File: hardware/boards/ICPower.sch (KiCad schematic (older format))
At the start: 39 parts, among them U1 ECP5UM5G-381caBGA, U3 CYUSB3014, U4 IS43TR16256B-125KBL, U5 128MiB, U6 128MiB

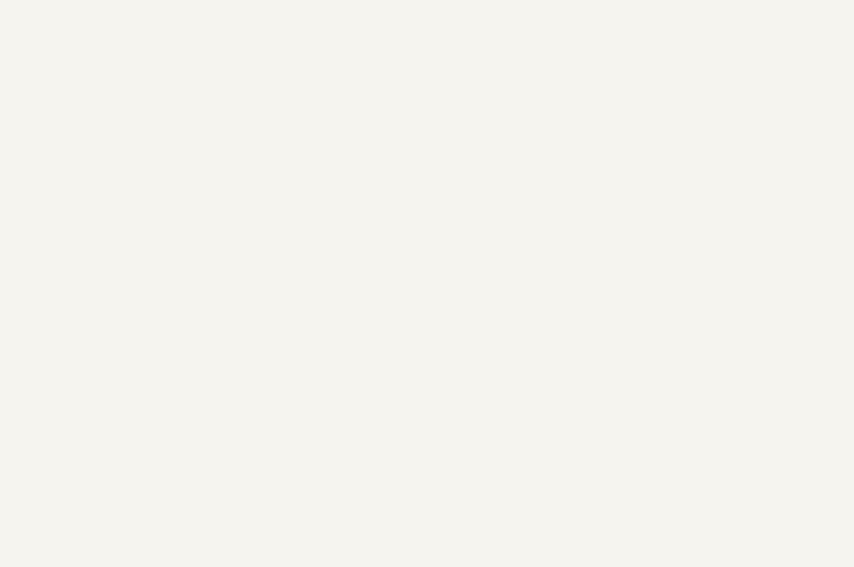
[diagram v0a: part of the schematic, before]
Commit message: Added a clock fanout buffer for the PCIe REFCLOCK to connect to the FPGAs SERDES banks
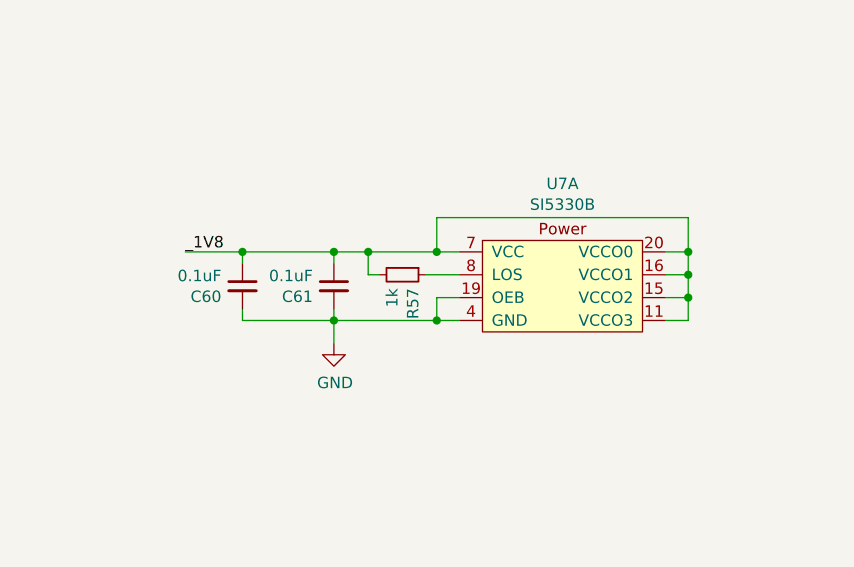
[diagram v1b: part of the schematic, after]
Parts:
- added C60, C61: 0.1uF, Capacitor_SMD:C_0603_1608Metric, symbol Device:C_Small
- added R57: 1k, Resistor_SMD:R_0603_1608Metric, symbol Device:R_Small
- added U7: SI5330B, Package_DFN_QFN:VQFN-24-1EP_4x4mm_P0.5mm_EP2.45x2.45mm, symbol lethalbit:SI5330B
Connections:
- net 1V8: now also C60.1, C61.1, R57.2, U7.11 (VCCO3), U7.15 (VCCO2), U7.16 (VCCO1), U7.20 (VCCO0), U7.24 (VCC), U7.7 (VCC)
- net GND: now also C60.2, C61.2, U7.12 (GND), U7.19 (OEB), U7.23 (GND), U7.25 (GND), U7.4 (GND), U7.5 (GND), U7.6 (GND)
- new net: R57.1, U7.8 (LOS)
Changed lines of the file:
@@
 Wire Wire Line
 	6400 4700 6650 4700
+$Comp
+L lethalbit:SI5330B U7
+U 1 1 5F1C6134
+P 5250 8250
+F 0 "U7" H 5250 8648 50  0000 C CNN
+F 1 "SI5330B" H 5250 8557 50  0000 C CNN
+F 2 "Package_DFN_QFN:VQFN-24-1EP_4x4mm_P0.5mm_EP2.45x2.45mm" H 5250 8550 50  0001 C CNN
+F 3 "https://www.silabs.com/documents/public/data-sheets/Si5330.pdf" H 5250 8550 50  0001 C CNN
+F 4 "Silicon Labs" H 5250 8250 50  0001 C CNN "MFR"
+F 5 "SI5330B-B00205-GM" H 5250 8250 50  0001 C CNN "MPN"
+	1    5250 8250
+	1    0    0    -1
+$EndComp
+$Comp
+L power:GND #PWR0141
+U 1 1 5F1E08C0
+P 4250 8550
+F 0 "#PWR0141" H 4250 8300 50  0001 C CNN
+F 1 "GND" H 4255 8377 50  0000 C CNN
+F 2 "" H 4250 8550 50  0001 C CNN
+F 3 "" H 4250 8550 50  0001 C CNN
+	1    4250 8550
+	1    0    0    -1
+$EndComp
+Wire Wire Line
+	4800 8450 4700 8450
+Wire Wire Line
+	4250 8450 4250 8550
+$Comp
+L Device:C_Small C?
+U 1 1 5F1EFE73
+P 4250 8300
+AR Path="/5EDF9F51/5F1EFE73" Ref="C?"  Part="1"
+AR Path="/5EF66188/5F1EFE73" Ref="C61"  Part="1"
+F 0 "C61" H 4158 8254 50  0000 R CNN
+F 1 "0.1uF" H 4158 8345 50  0000 R CNN
+F 2 "Capacitor_SMD:C_0603_1608Metric" H 4250 8300 50  0001 C CNN
+F 3 "~" H 4250 8300 50  0001 C CNN
+F 4 "KEMET" V 4250 8300 50  0001 C CNN "MFR"
+F 5 "C0603C104M5RACTU" V 4250 8300 50  0001 C CNN "MPN"
+	1    4250 8300
+	1    0    0    -1
+$EndComp
+Wire Wire Line
+	4250 8400 4250 8450
+Wire Wire Line
+	4250 8200 4250 8150
+Wire Wire Line
+	4250 8150 4400 8150
+Wire Wire Line
+	4250 8150 3850 8150
+Connection ~ 4250 8150
+Text Label 3600 8150 0    50   ~ 0
+_1V8
+Wire Wire Line
+	4700 8150 4700 8000
+Wire Wire Line
+	4700 8000 5800 8000
+Wire Wire Line
+	5800 8000 5800 8150
+Wire Wire Line
+	5800 8450 5700 8450
+Connection ~ 4700 8150
+Wire Wire Line
+	4700 8150 4800 8150
+Wire Wire Line
+	5800 8350 5700 8350
+Connection ~ 5800 8350
+Wire Wire Line
+	5800 8350 5800 8450
+Wire Wire Line
+	5800 8250 5700 8250
+Connection ~ 5800 8250
+Wire Wire Line
+	5800 8250 5800 8350
+Wire Wire Line
+	5800 8150 5700 8150
+Connection ~ 5800 8150
+Wire Wire Line
+	5800 8150 5800 8250
+$Comp
+L Device:R_Small R?
+U 1 1 5F29D318
+P 4550 8250
+AR Path="/5EF66251/5F29D318" Ref="R?"  Part="1"
+AR Path="/5EF66188/5F29D318" Ref="R57"  Part="1"
+F 0 "R57" H 4609 8296 50  0000 L CNN
+F 1 "1k" H 4609 8205 50  0000 L CNN
+F 2 "Resistor_SMD:R_0603_1608Metric" H 4550 8250 50  0001 C CNN
+F 3 "~" H 4550 8250 50  0001 C CNN
+F 4 "Vishay Dale" H 4550 8250 50  0001 C CNN "MFR"
+F 5 "CRCW06031K00FKEAHP" H 4550 8250 50  0001 C CNN "MPN"
+	1    4550 8250
+	0    1    1    0
+$EndComp
+Connection ~ 4250 8450
+Wire Wire Line
+	4400 8150 4400 8250
+Wire Wire Line
+	4400 8250 4450 8250
+Connection ~ 4400 8150
+Wire Wire Line
+	4400 8150 4700 8150
+Wire Wire Line
+	4650 8250 4800 8250
+Wire Wire Line
+	4800 8350 4700 8350
+Wire Wire Line
+	4700 8350 4700 8450
+Connection ~ 4700 8450
+Wire Wire Line
+	4700 8450 4250 8450
+$Comp
+L Device:C_Small C?
+U 1 1 5F326C43
+P 3850 8300
+AR Path="/5EDF9F51/5F326C43" Ref="C?"  Part="1"
+AR Path="/5EF66188/5F326C43" Ref="C60"  Part="1"
+F 0 "C60" H 3758 8254 50  0000 R CNN
+F 1 "0.1uF" H 3758 8345 50  0000 R CNN
+F 2 "Capacitor_SMD:C_0603_1608Metric" H 3850 8300 50  0001 C CNN
+F 3 "~" H 3850 8300 50  0001 C CNN
+F 4 "KEMET" V 3850 8300 50  0001 C CNN "MFR"
+F 5 "C0603C104M5RACTU" V 3850 8300 50  0001 C CNN "MPN"
+	1    3850 8300
+	1    0    0    -1
+$EndComp
+Wire Wire Line
+	3850 8150 3850 8200
+Connection ~ 3850 8150
+Wire Wire Line
+	3850 8150 3600 8150
+Wire Wire Line
+	3850 8400 3850 8450
+Wire Wire Line
+	3850 8450 4250 8450
 $EndSCHEMATC

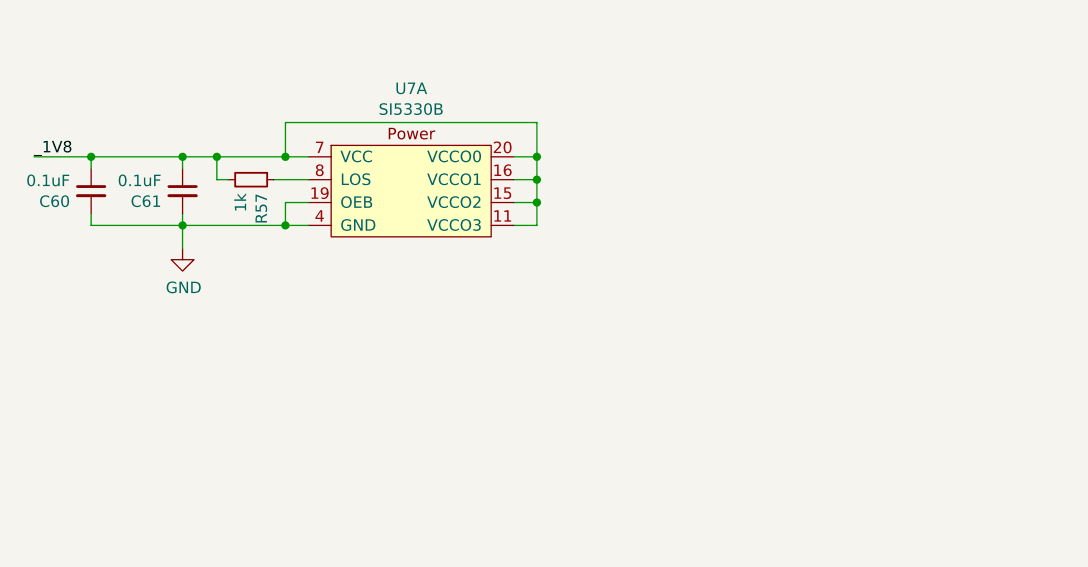
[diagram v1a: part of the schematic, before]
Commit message: Added missing bypass caps for the VCCO rails for the clock buffer
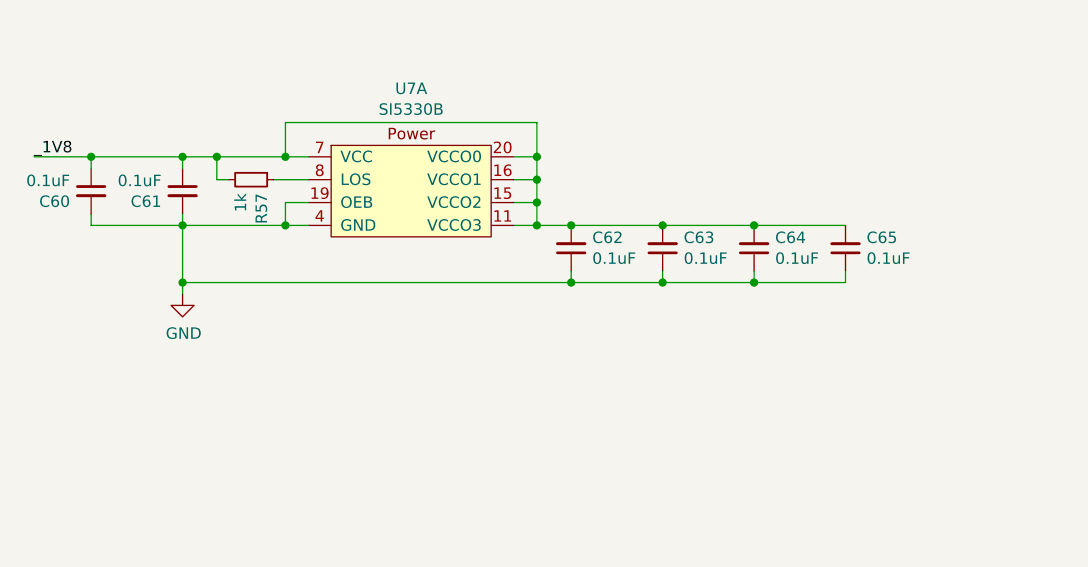
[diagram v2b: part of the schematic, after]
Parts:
- added C62, C63, C64, C65: 0.1uF, Capacitor_SMD:C_0603_1608Metric, symbol Device:C_Small
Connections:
- net 1V8: now also C62.2, C63.2, C64.2, C65.2
- net GND: now also C62.1, C63.1, C64.1, C65.1
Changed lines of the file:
@@
 L power:GND #PWR0141
 U 1 1 5F1E08C0
-P 4250 8550
-F 0 "#PWR0141" H 4250 8300 50  0001 C CNN
-F 1 "GND" H 4255 8377 50  0000 C CNN
-F 2 "" H 4250 8550 50  0001 C CNN
-F 3 "" H 4250 8550 50  0001 C CNN
-	1    4250 8550
+P 4250 8750
+F 0 "#PWR0141" H 4250 8500 50  0001 C CNN
+F 1 "GND" H 4255 8577 50  0000 C CNN
+F 2 "" H 4250 8750 50  0001 C CNN
+F 3 "" H 4250 8750 50  0001 C CNN
+	1    4250 8750
 	1    0    0    -1
 $EndComp
@@
 	4800 8450 4700 8450
 Wire Wire Line
-	4250 8450 4250 8550
+	4250 8450 4250 8700
 $Comp
 L Device:C_Small C?
@@
 Wire Wire Line
 	3850 8450 4250 8450
+$Comp
+L Device:C_Small C?
+U 1 1 5F3D3DC2
+P 5950 8550
+AR Path="/5EDF9F51/5F3D3DC2" Ref="C?"  Part="1"
+AR Path="/5EF66188/5F3D3DC2" Ref="C62"  Part="1"
+F 0 "C62" H 5858 8504 50  0000 R CNN
+F 1 "0.1uF" H 5858 8595 50  0000 R CNN
+F 2 "Capacitor_SMD:C_0603_1608Metric" H 5950 8550 50  0001 C CNN
+F 3 "~" H 5950 8550 50  0001 C CNN
+F 4 "KEMET" V 5950 8550 50  0001 C CNN "MFR"
+F 5 "C0603C104M5RACTU" V 5950 8550 50  0001 C CNN "MPN"
+	1    5950 8550
+	-1   0    0    1
+$EndComp
+$Comp
+L Device:C_Small C?
+U 1 1 5F3D4D67
+P 6350 8550
+AR Path="/5EDF9F51/5F3D4D67" Ref="C?"  Part="1"
+AR Path="/5EF66188/5F3D4D67" Ref="C63"  Part="1"
+F 0 "C63" H 6258 8504 50  0000 R CNN
+F 1 "0.1uF" H 6258 8595 50  0000 R CNN
+F 2 "Capacitor_SMD:C_0603_1608Metric" H 6350 8550 50  0001 C CNN
+F 3 "~" H 6350 8550 50  0001 C CNN
+F 4 "KEMET" V 6350 8550 50  0001 C CNN "MFR"
+F 5 "C0603C104M5RACTU" V 6350 8550 50  0001 C CNN "MPN"
+	1    6350 8550
+	-1   0    0    1
+$EndComp
+$Comp
+L Device:C_Small C?
+U 1 1 5F3D5176
+P 6750 8550
+AR Path="/5EDF9F51/5F3D5176" Ref="C?"  Part="1"
+AR Path="/5EF66188/5F3D5176" Ref="C64"  Part="1"
+F 0 "C64" H 6658 8504 50  0000 R CNN
+F 1 "0.1uF" H 6658 8595 50  0000 R CNN
+F 2 "Capacitor_SMD:C_0603_1608Metric" H 6750 8550 50  0001 C CNN
+F 3 "~" H 6750 8550 50  0001 C CNN
+F 4 "KEMET" V 6750 8550 50  0001 C CNN "MFR"
+F 5 "C0603C104M5RACTU" V 6750 8550 50  0001 C CNN "MPN"
+	1    6750 8550
+	-1   0    0    1
+$EndComp
+$Comp
+L Device:C_Small C?
+U 1 1 5F3D5646
+P 7150 8550
+AR Path="/5EDF9F51/5F3D5646" Ref="C?"  Part="1"
+AR Path="/5EF66188/5F3D5646" Ref="C65"  Part="1"
+F 0 "C65" H 7058 8504 50  0000 R CNN
+F 1 "0.1uF" H 7058 8595 50  0000 R CNN
+F 2 "Capacitor_SMD:C_0603_1608Metric" H 7150 8550 50  0001 C CNN
+F 3 "~" H 7150 8550 50  0001 C CNN
+F 4 "KEMET" V 7150 8550 50  0001 C CNN "MFR"
+F 5 "C0603C104M5RACTU" V 7150 8550 50  0001 C CNN "MPN"
+	1    7150 8550
+	-1   0    0    1
+$EndComp
+Wire Wire Line
+	5800 8450 5950 8450
+Connection ~ 5800 8450
+Connection ~ 5950 8450
+Wire Wire Line
+	5950 8450 6350 8450
+Connection ~ 6350 8450
+Wire Wire Line
+	6350 8450 6750 8450
+Connection ~ 6750 8450
+Wire Wire Line
+	6750 8450 7150 8450
+Wire Wire Line
+	4250 8700 5950 8700
+Wire Wire Line
+	7150 8700 7150 8650
+Connection ~ 4250 8700
+Wire Wire Line
+	4250 8700 4250 8750
+Wire Wire Line
+	6750 8650 6750 8700
+Connection ~ 6750 8700
+Wire Wire Line
+	6750 8700 7150 8700
+Wire Wire Line
+	6350 8650 6350 8700
+Connection ~ 6350 8700
+Wire Wire Line
+	6350 8700 6750 8700
+Wire Wire Line
+	5950 8650 5950 8700
+Connection ~ 5950 8700
+Wire Wire Line
+	5950 8700 6350 8700
 $EndSCHEMATC

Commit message: A batch of misc changes, I don't exactly recall what changed
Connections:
- net 1V5: now also U1.H14 (VCCIO2), U1.H15 (VCCIO2), U1.J15 (VCCIO2), U1.L14 (VCCIO3), U1.L15 (VCCIO3), U1.M15 (VCCIO3); no longer U1.H6 (VCCIO7), U1.H7 (VCCIO7), U1.J6 (VCCIO7), U1.L6 (VCCIO6), U1.L7 (VCCIO6), U1.M6 (VCCIO6)
- net 1V8: now also U1.H6 (VCCIO7), U1.H7 (VCCIO7), U1.J6 (VCCIO7)
- new net: U1.L6 (VCCIO6), U1.L7 (VCCIO6), U1.M6 (VCCIO6)
- no-connect marks 9 -> 8
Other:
- moved on the sheet: C47, C48, C49, C50, C51, C52
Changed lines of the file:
@@
 NoConn ~ 9100 2000
 NoConn ~ 9100 2150
-NoConn ~ 9100 2300
-NoConn ~ 9100 2450
 $Comp
 L Device:C_Small C40
@@
 	9700 8000 9750 8000
 Wire Wire Line
-	9100 2750 10200 2750
-Wire Wire Line
-	9100 2600 11100 2600
-Wire Wire Line
-	11100 2750 11100 2600
-Connection ~ 11100 2600
-Wire Wire Line
-	11100 2600 11400 2600
-Text Label 12550 2600 2    50   ~ 0
+	9100 2450 10200 2450
+Wire Wire Line
+	9100 2300 11100 2300
+Wire Wire Line
+	11100 2450 11100 2300
+Connection ~ 11100 2300
+Wire Wire Line
+	11100 2300 11400 2300
+Text Label 12550 2300 2    50   ~ 0
 _1V5
 $Comp
 L Device:C_Small C48
 U 1 1 5FA901F7
-P 10600 2850
-F 0 "C48" H 10692 2896 50  0000 L CNN
-F 1 "100nF" H 10692 2805 50  0000 L CNN
-F 2 "Capacitor_SMD:C_0402_1005Metric" H 10600 2850 50  0001 C CNN
-F 3 "~" H 10600 2850 50  0001 C CNN
-F 4 "KEMET" H 10600 2850 50  0001 C CNN "MFR"
-F 5 "C0402C104M8PACTU" H 10600 2850 50  0001 C CNN "MPN"
-	1    10600 2850
-	1    0    0    -1
-$EndComp
-Connection ~ 10600 2750
-Wire Wire Line
-	10600 2750 11050 2750
+P 10600 2550
+F 0 "C48" H 10692 2596 50  0000 L CNN
+F 1 "100nF" H 10692 2505 50  0000 L CNN
+F 2 "Capacitor_SMD:C_0402_1005Metric" H 10600 2550 50  0001 C CNN
+F 3 "~" H 10600 2550 50  0001 C CNN
+F 4 "KEMET" H 10600 2550 50  0001 C CNN "MFR"
+F 5 "C0402C104M8PACTU" H 10600 2550 50  0001 C CNN "MPN"
+	1    10600 2550
+	1    0    0    -1
+$EndComp
+Connection ~ 10600 2450
+Wire Wire Line
+	10600 2450 11050 2450
 $Comp
 L Device:C_Small C47
 U 1 1 5FA94FC6
-P 10200 2850
-F 0 "C47" H 10292 2896 50  0000 L CNN
-F 1 "10nF" H 10292 2805 50  0000 L CNN
-F 2 "Capacitor_SMD:C_0402_1005Metric" H 10200 2850 50  0001 C CNN
-F 3 "~" H 10200 2850 50  0001 C CNN
-F 4 "KEMET" H 10200 2850 50  0001 C CNN "MFR"
-F 5 "C0402C103M5RACTU" H 10200 2850 50  0001 C CNN "MPN"
-	1    10200 2850
-	1    0    0    -1
-$EndComp
-Connection ~ 10200 2750
-Wire Wire Line
-	10200 2750 10600 2750
+P 10200 2550
+F 0 "C47" H 10292 2596 50  0000 L CNN
+F 1 "10nF" H 10292 2505 50  0000 L CNN
+F 2 "Capacitor_SMD:C_0402_1005Metric" H 10200 2550 50  0001 C CNN
+F 3 "~" H 10200 2550 50  0001 C CNN
+F 4 "KEMET" H 10200 2550 50  0001 C CNN "MFR"
+F 5 "C0402C103M5RACTU" H 10200 2550 50  0001 C CNN "MPN"
+	1    10200 2550
+	1    0    0    -1
+$EndComp
+Connection ~ 10200 2450
+Wire Wire Line
+	10200 2450 10600 2450
 $Comp
 L Device:C_Small C49
 U 1 1 5FABEDAF
-P 11050 2850
-F 0 "C49" H 11142 2896 50  0000 L CNN
-F 1 "10nF" H 11142 2805 50  0000 L CNN
-F 2 "Capacitor_SMD:C_0402_1005Metric" H 11050 2850 50  0001 C CNN
-F 3 "~" H 11050 2850 50  0001 C CNN
-F 4 "KEMET" H 11050 2850 50  0001 C CNN "MFR"
-F 5 "C0402C103M5RACTU" H 11050 2850 50  0001 C CNN "MPN"
-	1    11050 2850
-	1    0    0    -1
-$EndComp
-Connection ~ 11050 2750
-Wire Wire Line
-	11050 2750 11100 2750
-Wire Wire Line
-	10200 2950 10200 3000
-Wire Wire Line
-	10200 3000 10600 3000
-Wire Wire Line
-	11050 3000 11050 2950
-Wire Wire Line
-	10600 2950 10600 3000
-Connection ~ 10600 3000
-Wire Wire Line
-	10600 3000 11050 3000
-Wire Wire Line
-	10200 3000 10200 3250
+P 11050 2550
+F 0 "C49" H 11142 2596 50  0000 L CNN
+F 1 "10nF" H 11142 2505 50  0000 L CNN
+F 2 "Capacitor_SMD:C_0402_1005Metric" H 11050 2550 50  0001 C CNN
+F 3 "~" H 11050 2550 50  0001 C CNN
+F 4 "KEMET" H 11050 2550 50  0001 C CNN "MFR"
+F 5 "C0402C103M5RACTU" H 11050 2550 50  0001 C CNN "MPN"
+	1    11050 2550
+	1    0    0    -1
+$EndComp
+Connection ~ 11050 2450
+Wire Wire Line
+	11050 2450 11100 2450
+Wire Wire Line
+	10200 2750 10600 2750
+Wire Wire Line
+	11050 2750 11050 2650
+Wire Wire Line
+	10600 2650 10600 2750
+Connection ~ 10600 2750
+Wire Wire Line
+	10600 2750 11050 2750
 Wire Wire Line
 	10200 3250 9900 3250
-Connection ~ 10200 3000
 Connection ~ 9900 3250
 $Comp
 L Device:C_Small C51
 U 1 1 5FAD68A7
-P 11800 2700
-F 0 "C51" H 11892 2746 50  0000 L CNN
-F 1 "100nF" H 11892 2655 50  0000 L CNN
-F 2 "Capacitor_SMD:C_0402_1005Metric" H 11800 2700 50  0001 C CNN
-F 3 "~" H 11800 2700 50  0001 C CNN
-F 4 "KEMET" H 11800 2700 50  0001 C CNN "MFR"
-F 5 "C0402C104M8PACTU" H 11800 2700 50  0001 C CNN "MPN"
-	1    11800 2700
+P 11800 2400
+F 0 "C51" H 11892 2446 50  0000 L CNN
+F 1 "100nF" H 11892 2355 50  0000 L CNN
+F 2 "Capacitor_SMD:C_0402_1005Metric" H 11800 2400 50  0001 C CNN
+F 3 "~" H 11800 2400 50  0001 C CNN
+F 4 "KEMET" H 11800 2400 50  0001 C CNN "MFR"
+F 5 "C0402C104M8PACTU" H 11800 2400 50  0001 C CNN "MPN"
+	1    11800 2400
 	1    0    0    -1
 $EndComp
@@
 L Device:C_Small C50
 U 1 1 5FAD68AF
-P 11400 2700
-F 0 "C50" H 11492 2746 50  0000 L CNN
-F 1 "10nF" H 11492 2655 50  0000 L CNN
-F 2 "Capacitor_SMD:C_0402_1005Metric" H 11400 2700 50  0001 C CNN
-F 3 "~" H 11400 2700 50  0001 C CNN
-F 4 "KEMET" H 11400 2700 50  0001 C CNN "MFR"
-F 5 "C0402C103M5RACTU" H 11400 2700 50  0001 C CNN "MPN"
-	1    11400 2700
+P 11400 2400
+F 0 "C50" H 11492 2446 50  0000 L CNN
+F 1 "10nF" H 11492 2355 50  0000 L CNN
+F 2 "Capacitor_SMD:C_0402_1005Metric" H 11400 2400 50  0001 C CNN
+F 3 "~" H 11400 2400 50  0001 C CNN
+F 4 "KEMET" H 11400 2400 50  0001 C CNN "MFR"
+F 5 "C0402C103M5RACTU" H 11400 2400 50  0001 C CNN "MPN"
+	1    11400 2400
 	1    0    0    -1
 $EndComp
@@
 L Device:C_Small C52
 U 1 1 5FAD68B7
-P 12250 2700
-F 0 "C52" H 12342 2746 50  0000 L CNN
-F 1 "10nF" H 12342 2655 50  0000 L CNN
-F 2 "Capacitor_SMD:C_0402_1005Metric" H 12250 2700 50  0001 C CNN
-F 3 "~" H 12250 2700 50  0001 C CNN
-F 4 "KEMET" H 12250 2700 50  0001 C CNN "MFR"
-F 5 "C0402C103M5RACTU" H 12250 2700 50  0001 C CNN "MPN"
-	1    12250 2700
-	1    0    0    -1
-$EndComp
-Connection ~ 11400 2600
-Wire Wire Line
-	11400 2600 11800 2600
-Connection ~ 11800 2600
-Wire Wire Line
-	11800 2600 12250 2600
-Connection ~ 12250 2600
-Wire Wire Line
-	12250 2600 12550 2600
-Wire Wire Line
-	11400 2800 11400 2850
-Wire Wire Line
-	11400 2850 11800 2850
-Wire Wire Line
-	12250 2850 12250 2800
-Wire Wire Line
-	11800 2800 11800 2850
-Connection ~ 11800 2850
-Wire Wire Line
-	11800 2850 12250 2850
-Wire Wire Line
-	11050 3000 11400 3000
-Wire Wire Line
-	11400 3000 11400 2850
-Connection ~ 11050 3000
-Connection ~ 11400 2850
+P 12250 2400
+F 0 "C52" H 12342 2446 50  0000 L CNN
+F 1 "10nF" H 12342 2355 50  0000 L CNN
+F 2 "Capacitor_SMD:C_0402_1005Metric" H 12250 2400 50  0001 C CNN
+F 3 "~" H 12250 2400 50  0001 C CNN
+F 4 "KEMET" H 12250 2400 50  0001 C CNN "MFR"
+F 5 "C0402C103M5RACTU" H 12250 2400 50  0001 C CNN "MPN"
+	1    12250 2400
+	1    0    0    -1
+$EndComp
+Connection ~ 11400 2300
+Wire Wire Line
+	11400 2300 11800 2300
+Connection ~ 11800 2300
+Wire Wire Line
+	11800 2300 12250 2300
+Connection ~ 12250 2300
+Wire Wire Line
+	12250 2300 12550 2300
+Wire Wire Line
+	11400 2500 11400 2550
+Wire Wire Line
+	11400 2550 11800 2550
+Wire Wire Line
+	12250 2550 12250 2500
+Wire Wire Line
+	11800 2500 11800 2550
+Connection ~ 11800 2550
+Wire Wire Line
+	11800 2550 12250 2550
+Wire Wire Line
+	11050 2750 11400 2750
+Wire Wire Line
+	11400 2750 11400 2550
+Connection ~ 11050 2750
+Connection ~ 11400 2550
 $Comp
 L Device:C_Small C?
@@
 Wire Wire Line
 	5950 8700 6350 8700
+Wire Wire Line
+	10200 2750 10200 3250
+Wire Wire Line
+	10200 2650 10200 2750
+Connection ~ 10200 2750
+Text Label 9600 2750 2    50   ~ 0
+_1V8
+Wire Wire Line
+	9100 2750 9600 2750
+NoConn ~ 9100 2600
 $EndSCHEMATC
